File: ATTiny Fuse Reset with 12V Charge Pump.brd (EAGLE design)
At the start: 21 parts, among them U2 ARDUINOR3-BPLACE, U3 ATTINY85-20PU

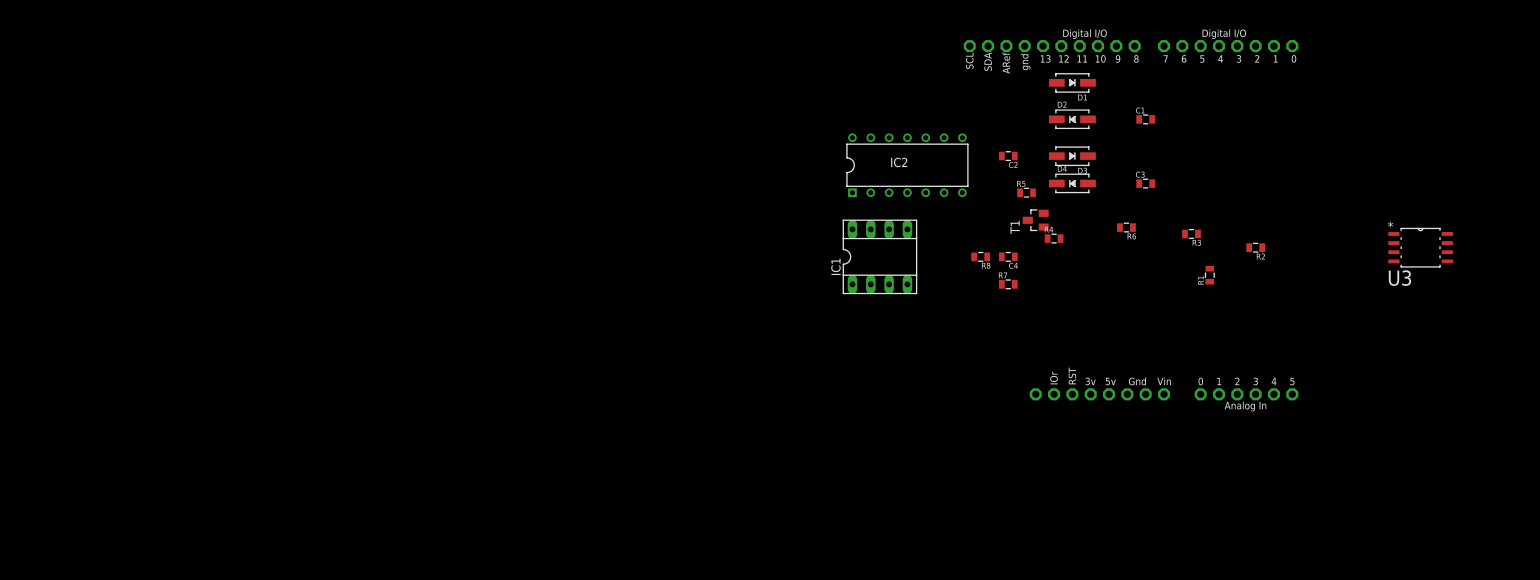
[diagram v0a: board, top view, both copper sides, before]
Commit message: need to add ISP header
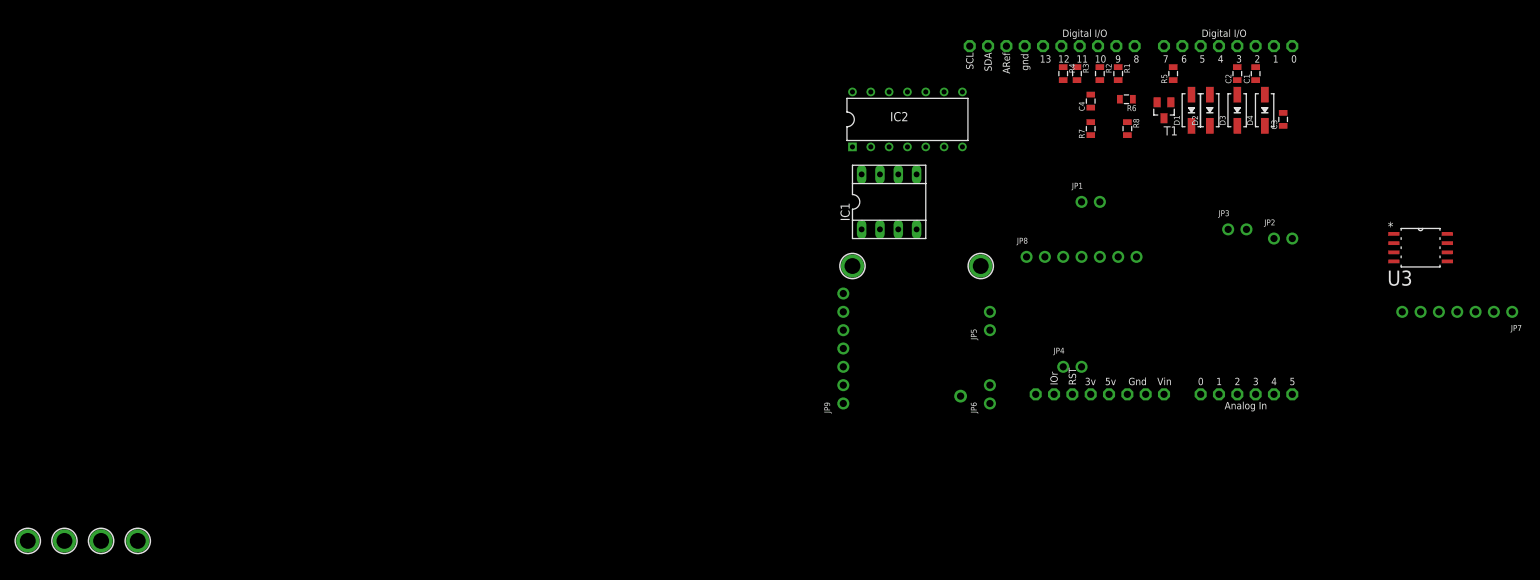
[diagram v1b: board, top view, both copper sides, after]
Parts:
- added JP1, JP2, JP3, JP4, JP5, JP6: (no value), ATtami:1X02_ROUND
- added JP10: (no value), ATtami:1X01-CLEANBIG
- added JP7, JP8, JP9: (no value), ATtami:1X07_ROUND
- added U$1, U$2, U$3, U$4, U$5, U$6: MOUNTINGHOLE2.0, ATtami:MOUNTINGHOLE_2.0_PLATED
- D1: value (none) -> 1N4148
- moved C2 33.7 mm to (55.9, 47.0), turned to 90 degrees
- moved R2 32.4 mm to (36.8, 47.0), turned to 270 degrees
- moved R1 30.7 mm to (39.4, 47.0), turned to 270 degrees
- moved D4 28.5 mm to (59.7, 41.9), turned to 90 degrees
- moved R3 27.3 mm to (33.7, 47.0), turned to 270 degrees
- moved R8 27.0 mm to (40.6, 39.4), turned to 270 degrees
- moved R5 26.2 mm to (47.0, 47.0), turned to 90 degrees
- moved C4 24.4 mm to (35.6, 43.2), turned to 90 degrees
- moved R7 24.4 mm to (35.6, 39.4), turned to 90 degrees
- moved D3 23.7 mm to (55.9, 41.9), turned to 90 degrees
- moved T1 23.4 mm to (45.7, 41.9), turned to 180 degrees
- moved R4 22.9 mm to (31.8, 47.0), turned to 270 degrees
- moved C3 21.0 mm to (62.2, 40.6), turned to 90 degrees
- moved D2 19.1 mm to (52.1, 41.9), turned to 90 degrees
- moved R6 17.8 mm to (40.5, 43.4)
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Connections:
- removed net N$13: D1.AQ
- removed net N$5: IC1.2, IC2.2, R4.2
- net N$14: now also IC1.2, IC2.2, R4.2
- net PUMP_VCC: now also D1.AQ

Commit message: added 1N4148 value
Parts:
- D2, D3, D4: value (none) -> 1N4148
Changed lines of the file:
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@@
 <element name="C4" library="ATtami" package="0805" value="2uF" x="35.56" y="43.18" rot="R90"/>
 <element name="D1" library="ATtami" package="SOD-323" value="1N4148" x="49.53" y="41.91" rot="R90"/>
-<element name="D2" library="ATtami" package="SOD-323" value="" x="52.07" y="41.91" rot="R90"/>
-<element name="D3" library="ATtami" package="SOD-323" value="" x="55.88" y="41.91" rot="R90"/>
-<element name="D4" library="ATtami" package="SOD-323" value="" x="59.69" y="41.91" rot="R90"/>
+<element name="D2" library="ATtami" package="SOD-323" value="1N4148" x="52.07" y="41.91" rot="R90"/>
+<element name="D3" library="ATtami" package="SOD-323" value="1N4148" x="55.88" y="41.91" rot="R90"/>
+<element name="D4" library="ATtami" package="SOD-323" value="1N4148" x="59.69" y="41.91" rot="R90"/>
 <element name="R1" library="ATtami" package="0805" value="1K" x="39.37" y="46.99" rot="R270"/>
 <element name="R2" library="ATtami" package="0805" value="1K" x="36.83" y="46.99" rot="R270"/>

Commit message: some caretaking
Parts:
- moved IC1 1.27 mm to (6.35, 29.2)
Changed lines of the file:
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@@
 <element name="T1" library="dp_devices" package="SOT-23" value="" x="45.72" y="41.91" rot="R180"/>
 <element name="U2" library="adafruit" package="ARDUINOR3-BPLACE" value="ARDUINOR3-BPLACE" x="0" y="0"/>
-<element name="IC1" library="reprap" package="SOCKET-08" value="" x="7.62" y="29.21"/>
+<element name="IC1" library="reprap" package="SOCKET-08" value="" x="6.35" y="29.21"/>
 <element name="U3" library="Atmel_By_element14_Batch_1-00" package="SOIC127P798X216-8N" value="ATTINY85-20PU" x="81.28" y="22.86">
 <attribute name="PACKAGE" value="SOIC-8" x="81.28" y="22.86" size="1.778" layer="27" display="off"/>
@@
 <wire x1="35.56" y1="44.08" x2="40.64" y2="40.27" width="0" layer="19" extent="1-1"/>
 <wire x1="26.416" y1="50.8" x2="35.56" y2="44.08" width="0" layer="19" extent="1-1"/>
-<wire x1="11.43" y1="25.4" x2="35.56" y2="44.08" width="0" layer="19" extent="1-1"/>
+<wire x1="10.16" y1="25.4" x2="35.56" y2="44.08" width="0" layer="19" extent="1-1"/>
 </signal>
 <signal name="VIN">
@@
 <contactref element="IC2" pad="1"/>
 <wire x1="2.54" y1="36.83" x2="41.656" y2="50.8" width="0" layer="19" extent="1-1"/>
-<wire x1="3.81" y1="33.02" x2="2.54" y2="36.83" width="0" layer="19" extent="1-1"/>
+<wire x1="2.54" y1="33.02" x2="2.54" y2="36.83" width="0" layer="19" extent="1-1"/>
 </signal>
 <signal name="N$2">
@@
 <contactref element="IC2" pad="7"/>
 <wire x1="17.78" y1="36.83" x2="39.37" y2="46.09" width="0" layer="19" extent="1-1"/>
-<wire x1="11.43" y1="33.02" x2="17.78" y2="36.83" width="0" layer="19" extent="1-1"/>
+<wire x1="10.16" y1="33.02" x2="17.78" y2="36.83" width="0" layer="19" extent="1-1"/>
 </signal>
 <signal name="N$3">
@@
 <contactref element="IC2" pad="8"/>
 <wire x1="17.78" y1="44.45" x2="36.83" y2="46.09" width="0" layer="19" extent="1-1"/>
-<wire x1="8.89" y1="33.02" x2="17.78" y2="44.45" width="0" layer="19" extent="1-1"/>
+<wire x1="7.62" y1="33.02" x2="17.78" y2="44.45" width="0" layer="19" extent="1-1"/>
 </signal>
 <signal name="N$10">
@@
 <wire x1="31.75" y1="46.09" x2="35.56" y2="42.28" width="0" layer="19" extent="1-1"/>
 <wire x1="5.08" y1="36.83" x2="31.75" y2="46.09" width="0" layer="19" extent="1-1"/>
-<wire x1="6.35" y1="25.4" x2="5.08" y2="36.83" width="0" layer="19" extent="1-1"/>
+<wire x1="5.08" y1="25.4" x2="5.08" y2="36.83" width="0" layer="19" extent="1-1"/>
 </signal>
 <signal name="P1">
@@
 <wire x1="41.413" y1="43.434" x2="44.77" y2="43.01" width="0" layer="19" extent="1-1"/>
 <wire x1="10.16" y1="36.83" x2="41.413" y2="43.434" width="0" layer="19" extent="1-1"/>
-<wire x1="3.81" y1="25.4" x2="10.16" y2="36.83" width="0" layer="19" extent="1-1"/>
+<wire x1="2.54" y1="25.4" x2="10.16" y2="36.83" width="0" layer="19" extent="1-1"/>
 </signal>
 <signal name="N$19">
@@
 <contactref element="R3" pad="2"/>
 <wire x1="15.24" y1="44.45" x2="33.655" y2="46.09" width="0" layer="19" extent="1-1"/>
-<wire x1="6.35" y1="33.02" x2="15.24" y2="44.45" width="0" layer="19" extent="1-1"/>
+<wire x1="5.08" y1="33.02" x2="15.24" y2="44.45" width="0" layer="19" extent="1-1"/>
 </signal>
 <signal name="PUMP_VCC">

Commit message: started library of parts
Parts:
- removed U3: ATTINY85-20PU, Atmel_By_element14_Batch_1-00:SOIC127P798X216-8N
- added C5: 0.2uF, ATtami:0805
- added D5: 1N4148, ATtami:SOD-323
- added JP11: (no value), SparkFun-Connectors:2X3-SHROUDED
- added JP12: (no value), microbuilder:2X05
- added LED1: (no value), ATtami:LED-805
- added R10: 10k, ATtami:0805
- added R9: 1K, ATtami:0805
- added U$7: SWITCH_SPDT, SparkFun-Electromechanical:KPS-1290
- moved U$6 212.9 mm to (88.9, 53.3)
- moved U$4 208.1 mm to (94.0, 53.3)
- moved U$5 206.4 mm to (88.9, 48.3)
- moved U$3 201.6 mm to (94.0, 48.3)
- moved JP7 83.8 mm to (2.54, 12.7), turned to 90 degrees
- moved JP10 74.0 mm to (88.6, 22.6)
- moved JP9 74.0 mm to (72.4, 29.2)
- moved U$1 74.0 mm to (91.4, 40.6)
- moved JP5 74.0 mm to (92.7, 33.0)
- moved JP6 74.0 mm to (92.7, 22.9)
- moved U$2 74.0 mm to (73.7, 40.6)
- moved JP2 43.2 mm to (22.9, 6.35), turned to 90 degrees
- moved JP1 36.6 mm to (5.08, 8.89), turned to 90 degrees
- moved JP3 34.2 mm to (22.9, 16.5), turned to 90 degrees
- moved JP4 30.7 mm to (5.08, 19.1), turned to 90 degrees
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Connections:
- removed net N$176: IC1.1, IC2.4, R6.1, T1.2
- new net N$4: LED1.C, R9.1
- new net N$5: D5.AQ, R10.2
- new net N$6: C5.1, U2.RESET
- new net N$7: C5.2, U$7.O
- new net N$9: U$7.S, U2.D6
- new net PB5: D5.CQ, IC1.1, IC2.4, JP11.5, JP12.5, R6.1, T1.2
- net ATTINY_VCC: now also LED1.A, R10.1
- net GND: now also JP11.6, JP12.10, JP12.4, JP12.6, JP12.8, R9.2, U$7.P
- net SDI: now also JP11.4, JP12.1
- net SDO: now also JP11.3, JP12.7
- net SII: now also JP11.1, JP12.9
- net VCC: now also JP11.2, JP12.2; no longer U3.8

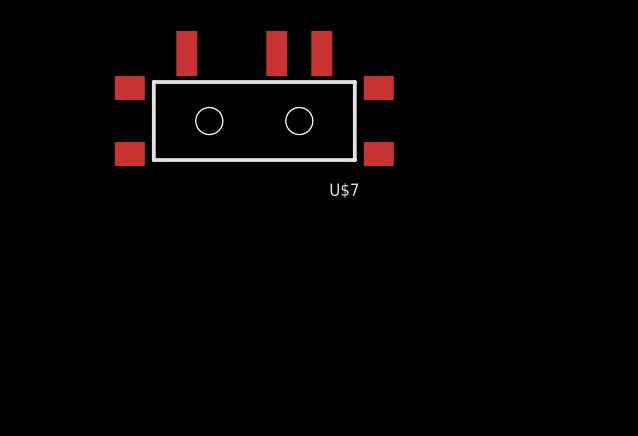
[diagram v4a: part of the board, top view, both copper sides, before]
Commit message: Added 12V protecting Zener
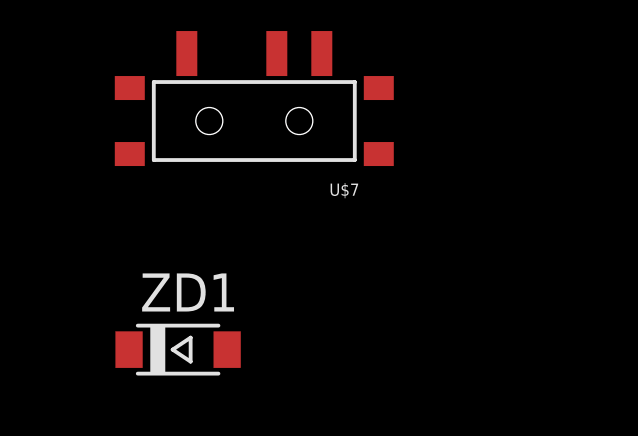
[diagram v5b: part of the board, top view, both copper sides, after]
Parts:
- added ZD1: 12V, dp_devices:SOD-123
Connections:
- net PB5 renamed RESET
- removed net 5V: U2.5V
- removed net GND1: U2.GND1
- removed net GND2: U2.GND2
- removed net N$1: IC2.11, IC2.12, IC2.13, IC2.14
- removed net N$3: IC1.6, IC2.8, R2.2
- new net N$13: IC1.6, R2.2
- net ATTINY_VCC: now also IC2.8
- net GND: now also IC2.11, IC2.12, IC2.13, IC2.14, U2.GND1, U2.GND2, ZD1.A
- net N$14: now also ZD1.C
- net VCC: now also U2.5V
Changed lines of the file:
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@@
 <element name="C5" library="ATtami" package="0805" value="0.2uF" x="-10.16" y="-5.08"/>
 <element name="U$7" library="SparkFun-Electromechanical" package="KPS-1290" value="SWITCH_SPDT" x="-5.08" y="-12.7"/>
+<element name="ZD1" library="dp_devices" package="SOD-123" value="12V" x="-7.62" y="-20.32"/>
 </elements>
 <signals>
@@
 <contactref element="JP12" pad="6"/>
 <contactref element="JP12" pad="8"/>
+<contactref element="U$7" pad="P"/>
+<contactref element="ZD1" pad="A"/>
 <contactref element="JP11" pad="6"/>
-<contactref element="U$7" pad="P"/>
+<contactref element="U2" pad="GND2"/>
+<contactref element="U2" pad="GND1"/>
+<contactref element="IC2" pad="13"/>
+<contactref element="IC2" pad="12"/>
+<contactref element="IC2" pad="14"/>
+<contactref element="IC2" pad="11"/>
 <wire x1="44.08" y1="38.1" x2="45.72" y2="40.81" width="0" layer="19" extent="1-1"/>
 <wire x1="40.64" y1="40.27" x2="44.08" y2="38.1" width="0" layer="19" extent="1-1"/>
@@
 <wire x1="25.4" y1="40.64" x2="35.56" y2="44.08" width="0" layer="19" extent="1-1"/>
 <wire x1="26.416" y1="50.8" x2="25.4" y2="40.64" width="0" layer="19" extent="1-1"/>
+<wire x1="11.43" y1="40.64" x2="25.4" y2="40.64" width="0" layer="19" extent="1-1"/>
+<wire x1="11.43" y1="38.1" x2="11.43" y2="40.64" width="0" layer="19" extent="1-1"/>
+<wire x1="11.43" y1="35.56" x2="11.43" y2="38.1" width="0" layer="19" extent="1-1"/>
+<wire x1="11.43" y1="33.02" x2="11.43" y2="35.56" width="0" layer="19" extent="1-1"/>
 <wire x1="43.18" y1="8.89" x2="44.08" y2="38.1" width="0" layer="19" extent="1-1"/>
 <wire x1="45.72" y1="8.89" x2="43.18" y2="8.89" width="0" layer="19" extent="1-1"/>
 <wire x1="48.26" y1="8.89" x2="45.72" y2="8.89" width="0" layer="19" extent="1-1"/>
 <wire x1="40.64" y1="8.89" x2="43.18" y2="8.89" width="0" layer="19" extent="1-1"/>
+<wire x1="43.18" y1="2.54" x2="43.18" y2="8.89" width="0" layer="19" extent="1-1"/>
+<wire x1="40.64" y1="2.54" x2="43.18" y2="2.54" width="0" layer="19" extent="1-1"/>
 <wire x1="58.42" y1="8.89" x2="48.26" y2="8.89" width="0" layer="19" extent="1-1"/>
-<wire x1="-4.33" y1="-10.45" x2="40.64" y2="8.89" width="0" layer="19" extent="1-1"/>
+<wire x1="-4.33" y1="-10.45" x2="11.43" y2="33.02" width="0" layer="19" extent="1-1"/>
+<wire x1="-5.985" y1="-20.32" x2="-4.33" y2="-10.45" width="0" layer="19" extent="1-1"/>
 </signal>
 <signal name="VIN">
 <contactref element="U2" pad="VIN"/>
 </signal>
-<signal name="GND1">
-<contactref element="U2" pad="GND1"/>
-</signal>
-<signal name="GND2">
-<contactref element="U2" pad="GND2"/>
-</signal>
-<signal name="5V">
-<contactref element="U2" pad="5V"/>
-</signal>
 <signal name="3V">
 <contactref element="U2" pad="3V"/>
@@
 <signal name="ATTINY_VCC">
 <contactref element="U2" pad="D8"/>
+<contactref element="R10" pad="1"/>
 <contactref element="IC1" pad="8"/>
 <contactref element="IC2" pad="1"/>
+<contactref element="IC2" pad="8"/>
 <contactref element="LED1" pad="A"/>
-<contactref element="R10" pad="1"/>
+<wire x1="30.48" y1="29.43" x2="41.656" y2="50.8" width="0" layer="19" extent="1-1"/>
 <wire x1="27.04" y1="25.4" x2="30.48" y2="29.43" width="0" layer="19" extent="1-1"/>
-<wire x1="41.656" y1="50.8" x2="27.04" y2="25.4" width="0" layer="19" extent="1-1"/>
-<wire x1="17.78" y1="33.02" x2="41.656" y2="50.8" width="0" layer="19" extent="1-1"/>
+<wire x1="17.78" y1="33.02" x2="27.04" y2="25.4" width="0" layer="19" extent="1-1"/>
+<wire x1="11.43" y1="25.4" x2="17.78" y2="33.02" width="0" layer="19" extent="1-1"/>
 <wire x1="3.81" y1="40.64" x2="17.78" y2="33.02" width="0" layer="19" extent="1-1"/>
 </signal>
 <signal name="N$2">
 <contactref element="R1" pad="2"/>
+<contactref element="IC2" pad="7"/>
 <contactref element="IC1" pad="5"/>
-<contactref element="IC2" pad="7"/>
 <wire x1="17.78" y1="40.64" x2="39.37" y2="46.09" width="0" layer="19" extent="1-1"/>
 <wire x1="3.81" y1="25.4" x2="17.78" y2="40.64" width="0" layer="19" extent="1-1"/>
-</signal>
-<signal name="N$3">
-<contactref element="R2" pad="2"/>
-<contactref element="IC1" pad="6"/>
-<contactref element="IC2" pad="8"/>
-<wire x1="17.78" y1="38.1" x2="36.83" y2="46.09" width="0" layer="19" extent="1-1"/>
-<wire x1="11.43" y1="25.4" x2="17.78" y2="38.1" width="0" layer="19" extent="1-1"/>
 </signal>
 <signal name="N$10">
@@
 <contactref element="R7" pad="2"/>
 <contactref element="R4" pad="2"/>
+<contactref element="IC2" pad="2"/>
+<contactref element="ZD1" pad="C"/>
 <contactref element="IC1" pad="2"/>
-<contactref element="IC2" pad="2"/>
 <wire x1="39.613" y1="43.434" x2="60.96" y2="44.069" width="0" layer="19" extent="1-1"/>
 <wire x1="35.56" y1="42.28" x2="39.613" y2="43.434" width="0" layer="19" extent="1-1"/>
@@
 <wire x1="25.4" y1="35.56" x2="35.56" y2="40.27" width="0" layer="19" extent="1-1"/>
 <wire x1="3.81" y1="38.1" x2="25.4" y2="35.56" width="0" layer="19" extent="1-1"/>
+<wire x1="-9.255" y1="-20.32" x2="3.81" y2="38.1" width="0" layer="19" extent="1-1"/>
 </signal>
 <signal name="P1">
@@
 <wire x1="55.88" y1="47.89" x2="55.88" y2="50.8" width="0" layer="19" extent="1-1"/>
 </signal>
-<signal name="PB5">
+<signal name="RESET">
 <contactref element="T1" pad="2"/>
 <contactref element="R6" pad="1"/>
-<contactref element="IC1" pad="1"/>
+<contactref element="JP12" pad="5"/>
+<contactref element="JP11" pad="5"/>
 <contactref element="IC2" pad="4"/>
 <contactref element="D5" pad="CQ"/>
-<contactref element="JP12" pad="5"/>
-<contactref element="JP11" pad="5"/>
+<contactref element="IC1" pad="1"/>
 <wire x1="41.413" y1="43.434" x2="44.77" y2="43.01" width="0" layer="19" extent="1-1"/>
 <wire x1="25.4" y1="33.02" x2="41.413" y2="43.434" width="0" layer="19" extent="1-1"/>
@@
 <wire x1="46.99" y1="47.89" x2="50.8" y2="50.8" width="0" layer="19" extent="1-1"/>
 </signal>
-<signal name="VCC">
-<contactref element="JP12" pad="2"/>
-<contactref element="JP11" pad="2"/>
-<wire x1="50.8" y1="8.89" x2="63.5" y2="8.89" width="0" layer="19" extent="1-1"/>
-</signal>
-<signal name="N$1">
-<contactref element="IC2" pad="14"/>
-<contactref element="IC2" pad="13"/>
-<contactref element="IC2" pad="12"/>
-<contactref element="IC2" pad="11"/>
-<wire x1="11.43" y1="38.1" x2="11.43" y2="40.64" width="0" layer="19" extent="1-1"/>
-<wire x1="11.43" y1="35.56" x2="11.43" y2="38.1" width="0" layer="19" extent="1-1"/>
-<wire x1="11.43" y1="33.02" x2="11.43" y2="35.56" width="0" layer="19" extent="1-1"/>
-</signal>
 <signal name="N$8">
 <contactref element="IC2" pad="9"/>
+<contactref element="R3" pad="2"/>
 <contactref element="IC1" pad="7"/>
-<contactref element="R3" pad="2"/>
 <wire x1="17.78" y1="35.56" x2="33.655" y2="46.09" width="0" layer="19" extent="1-1"/>
 <wire x1="11.43" y1="27.94" x2="17.78" y2="35.56" width="0" layer="19" extent="1-1"/>
@@
 <wire x1="30.48" y1="31.53" x2="42.28" y2="38.1" width="0" layer="19" extent="1-1"/>
 </signal>
-<signal name="N$5">
-<contactref element="D5" pad="AQ"/>
-<contactref element="R10" pad="2"/>
-<wire x1="25.4" y1="25.781" x2="28.84" y2="25.4" width="0" layer="19" extent="1-1"/>
-</signal>
 <signal name="N$6">
 <contactref element="U2" pad="RESET"/>
@@
 </signal>
 <signal name="N$9">
+<contactref element="U$7" pad="S"/>
 <contactref element="U2" pad="D6"/>
-<contactref element="U$7" pad="S"/>
 <wire x1="-2.83" y1="-10.45" x2="48.26" y2="50.8" width="0" layer="19" extent="1-1"/>
 </signal>
@@
 <wire x1="-9.26" y1="-5.08" x2="-7.33" y2="-10.45" width="0" layer="19" extent="1-1"/>
 </signal>
+<signal name="N$5">
+<contactref element="R10" pad="2"/>
+<contactref element="D5" pad="AQ"/>
+<wire x1="25.4" y1="25.781" x2="28.84" y2="25.4" width="0" layer="19" extent="1-1"/>
+</signal>
+<signal name="N$13">
+<contactref element="IC1" pad="6"/>
+<contactref element="R2" pad="2"/>
+<wire x1="17.78" y1="38.1" x2="36.83" y2="46.09" width="0" layer="19" extent="1-1"/>
+</signal>
+<signal name="VCC">
+<contactref element="JP12" pad="2"/>
+<contactref element="JP11" pad="2"/>
+<contactref element="U2" pad="5V"/>
+<wire x1="50.8" y1="8.89" x2="63.5" y2="8.89" width="0" layer="19" extent="1-1"/>
+<wire x1="38.1" y1="2.54" x2="50.8" y2="8.89" width="0" layer="19" extent="1-1"/>
+</signal>
 </signals>
